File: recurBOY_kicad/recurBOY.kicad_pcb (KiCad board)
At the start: 2 copper layers, 100 x 100 mm, 39 parts, among them J1 CV_IN_0, J10 EURO_POWER, J2 CV_IN_1, J3 CV_IN_2, J4 CV_IN_3, J5 DISPLAY_1.8, J6 Conn_01x01, J7 VIDEO_OUT, J8 Raspberry_Pi_2_3, J9 BUTTON_NAV, SW1 BUTTON_1, SW2 BUTTON_2, SW3 BUTTON_3, SW4 BUTTON_4, SW5 BUTTON_5, U1 MCP3208

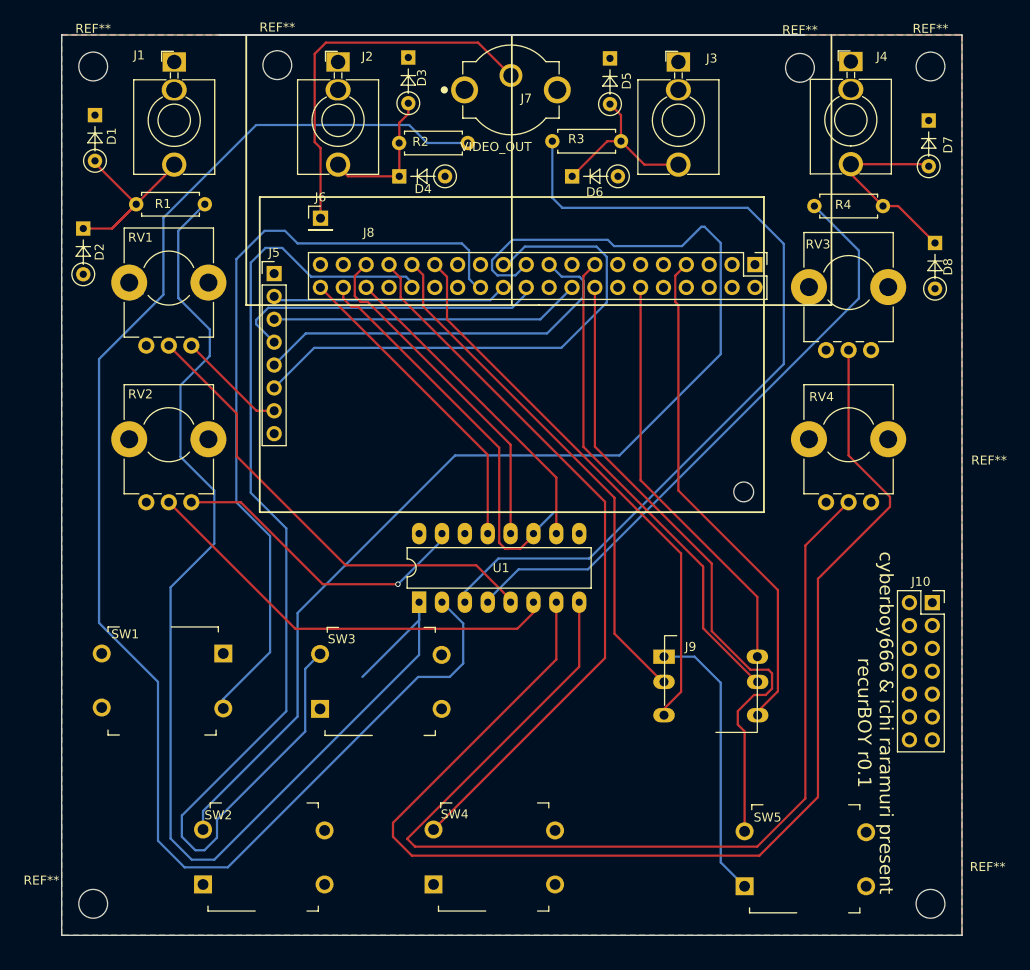
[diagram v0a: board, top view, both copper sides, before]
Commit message: updated kicad files and added booklet info
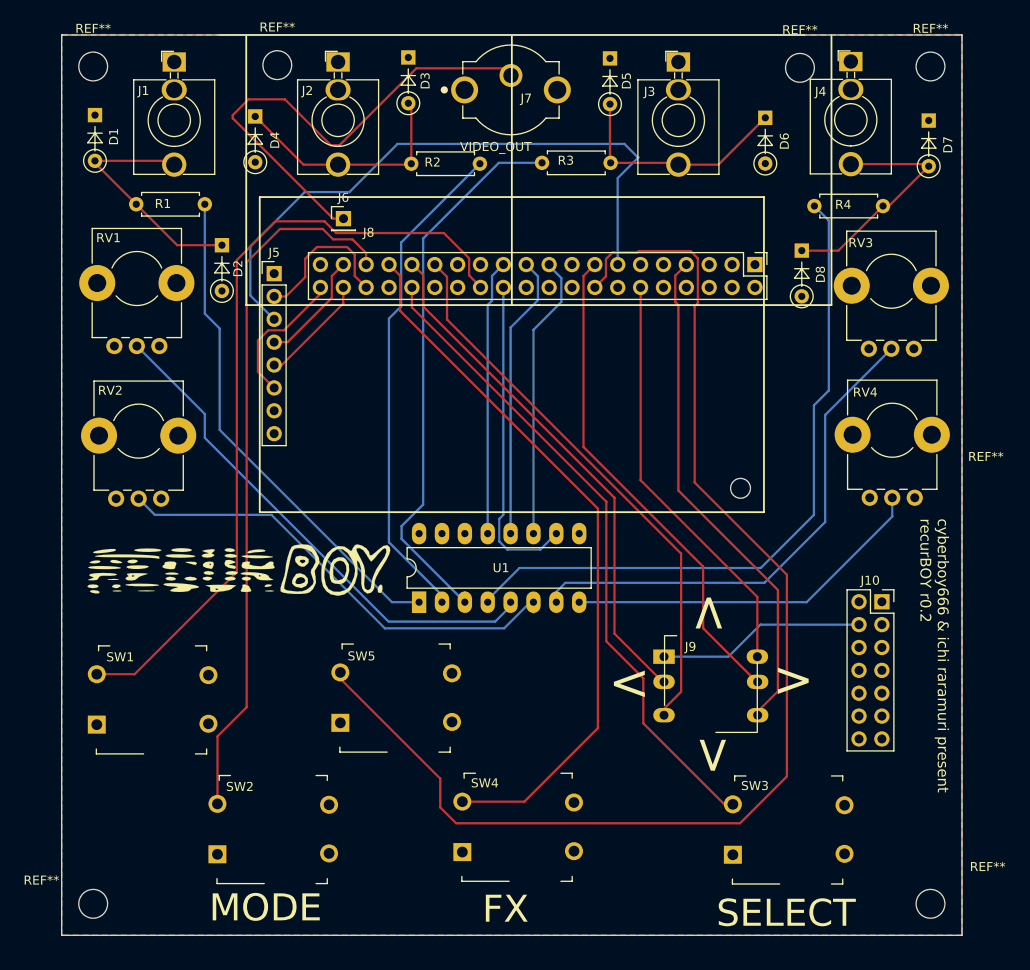
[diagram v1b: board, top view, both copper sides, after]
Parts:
- added G***: LOGO, custom_new:logo, F.Cu at (125.2, 94.8)
- moved SW5 48.9 mm to (135.3, 113.2)
- moved SW3 48.2 mm to (178.9, 127.8)
- moved D6 22.4 mm to (183.2, 44.2), turned to 270 degrees
- moved SW1 18.4 mm to (108.3, 113.4), turned to 90 degrees
- moved D4 17.3 mm to (126.5, 44.0), turned to 270 degrees
- moved D2 15.5 mm to (122.8, 58.4)
- moved D8 14.8 mm to (187.2, 59.0)
- moved J10 5.60 mm to (196.1, 98.0)
- moved RV4 4.88 mm to (199.8, 86.4)
- moved RV3 4.75 mm to (199.7, 69.8)
- moved SW4 4.20 mm to (148.9, 127.5)
- moved RV1 3.55 mm to (115.8, 69.5)
- moved RV2 3.37 mm to (116.0, 86.5)
- moved SW2 3.21 mm to (121.7, 127.8)
- moved R2 2.67 mm to (151.4, 49.3)
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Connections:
- J8 pad 13: Net-(J8-Pad13) -> DISPLAY_DC
- J8 pad 18: DISPLAY_DC -> Net-(J8-Pad18)
- J8 pad 19: DISPLAY_SDA -> D_IN
- J8 pad 21: BUTTON_IN_2 -> D_OUT
- J8 pad 22: DISPLAY_RST -> Net-(J8-Pad22)
- J8 pad 23: DISPLAY_SCL -> CLK
- J8 pad 24: DISPLAY_CS -> CS
- J8 pad 35: D_OUT -> BUTTON_IN_2
- J8 pad 36: CS -> DISPLAY_CS
- J8 pad 37: Net-(J8-Pad37) -> DISPLAY_RST
- J8 pad 38: D_IN -> DISPLAY_SDA
- J8 pad 40: CLK -> DISPLAY_SCL
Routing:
- net A_IN_1: track 166.7 -> 55.3 mm
- net A_IN_6: track 139.2 -> 56.5 mm
- net A_IN_0: track 132.8 -> 55.8 mm
- net A_IN_7: track 115.9 -> 40.8 mm
- net BUTTON_IN_5: track 72.4 -> 137.5 mm
- net BUTTON_IN_2: track 133.6 -> 78.7 mm
- net BUTTON_IN_3: track 121.2 -> 73.3 mm
- net +5V: track 46.6 -> 0.73 mm, vias 1 -> 0
- net DISPLAY_SCL: track 59.2 -> 16.3 mm
- net DISPLAY_DC: track 34.6 -> 70.5 mm
- net A_IN_2: track 94.5 -> 62.1 mm
- net DISPLAY_SDA: track 43.8 -> 12.3 mm
- net DISPLAY_RST: track 35.2 -> 12.7 mm
- net D_IN: track 45.1 -> 32.0 mm
- net Net-(J6-Pad1): track 42.3 -> 54.9 mm
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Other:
- board text added: ">"
- board text added: "FX"
- board text added: "MODE"
- board text added: "SELECT"
- board text added: "cyberboy666 & ichi raramuri present recurBOY r0.2"
- board text removed: "cyberboy666 & ichi raramuri present recurBOY r0.1"
